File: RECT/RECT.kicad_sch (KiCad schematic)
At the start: 10 parts, among them J1 AudioJack2_SwitchT, J2 AudioJack2_SwitchT, J3 AudioJack2_SwitchT, J4 AudioJack2_SwitchT, Q1 BSS84, Q2 BSS84, Q3 2N7002, Q4 2N7002

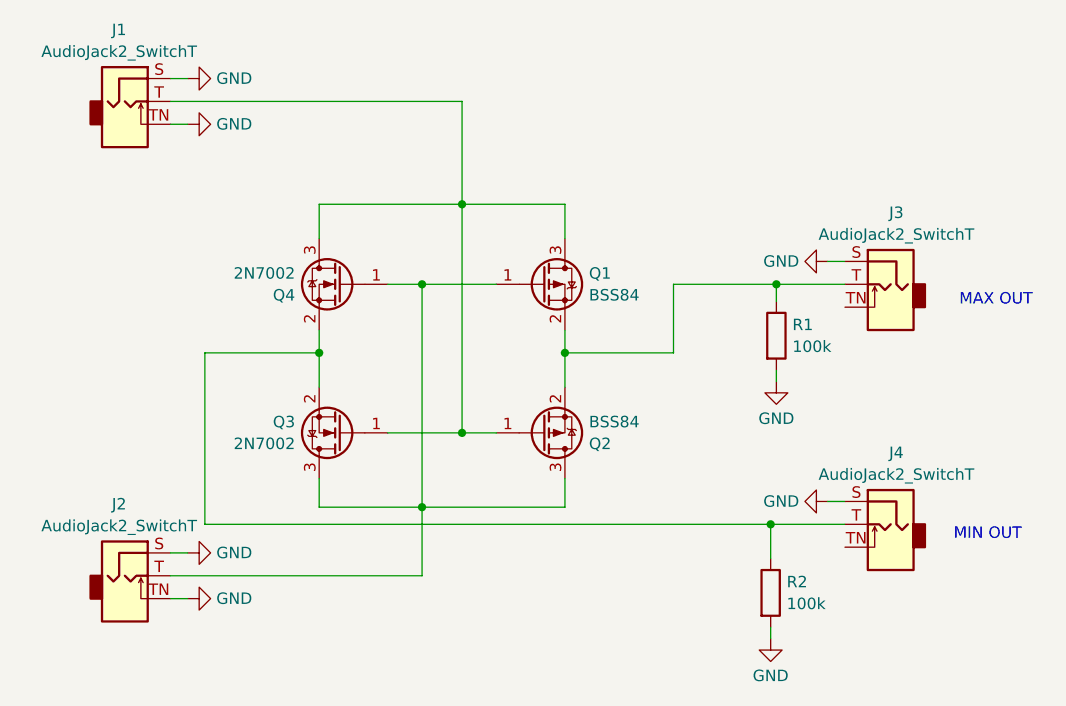
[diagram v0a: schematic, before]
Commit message: Increase impedance
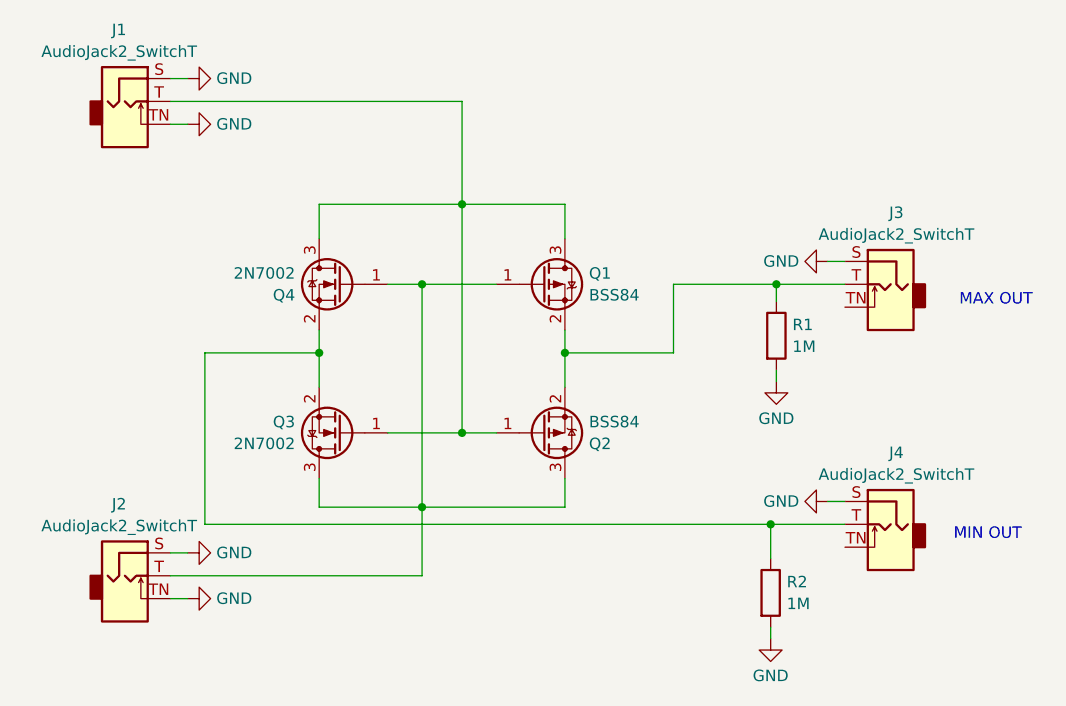
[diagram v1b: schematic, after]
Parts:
- R1, R2: value 100k -> 1M
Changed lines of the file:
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@@
       (effects (font (size 1.27 1.27)) (justify left))
     )
-    (property "Value" "100k" (at 158.623 108.5271 0)
+    (property "Value" "1M" (at 158.623 108.5271 0)
       (effects (font (size 1.27 1.27)) (justify left))
     )
@@
       (effects (font (size 1.27 1.27)) (justify left))
     )
-    (property "Value" "100k" (at 159.258 79.9521 0)
+    (property "Value" "1M" (at 159.258 79.9521 0)
       (effects (font (size 1.27 1.27)) (justify left))
     )

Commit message: Layout RECT
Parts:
- J1, J2, J3, J4: footprint (none) -> Custom_FP:PJ398SM
- R1, R2: footprint (none) -> Resistor_SMD:R_0603_1608Metric
